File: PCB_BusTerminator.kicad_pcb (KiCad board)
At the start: 2 copper layers, 16 x 33 mm, 5 parts, among them J1 Interconnect Bus

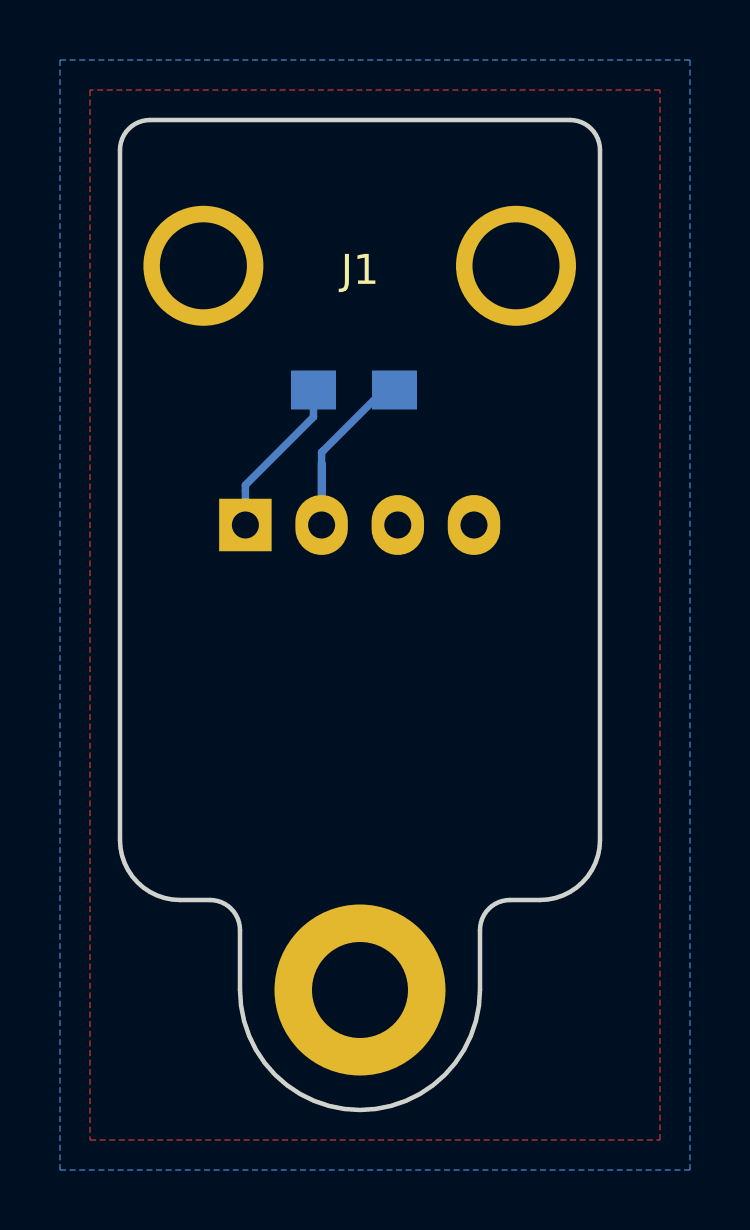
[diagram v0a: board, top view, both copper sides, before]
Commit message: Move top edge closer to connector
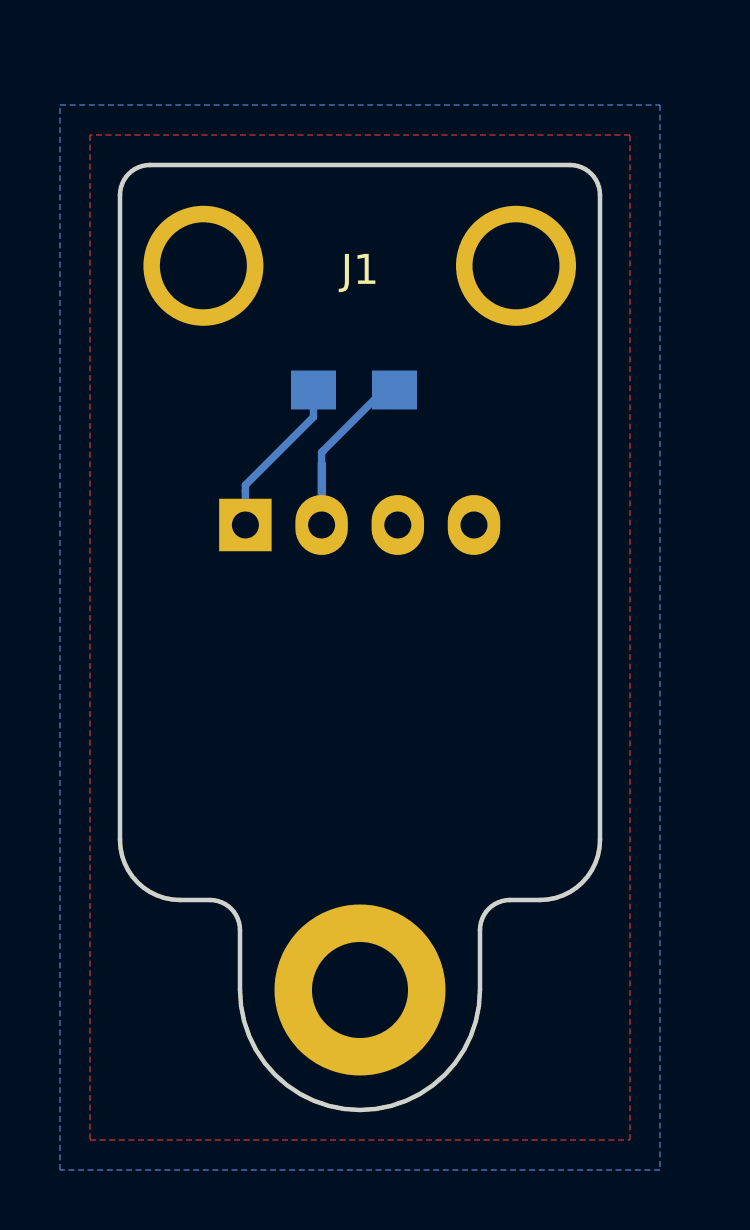
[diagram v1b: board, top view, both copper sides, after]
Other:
- board size 16 x 33 mm -> 16 x 31.5 mm
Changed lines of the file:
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@@
     (links 2)
     (no_connects 0)
-    (area 143.924999 107.924999 160.075001 141.075001)
+    (area 143.924999 109.424999 160.075001 141.075001)
     (thickness 1.6)
     (drawings 15)
@@
     (effects (font (size 1.1 1.1) (thickness 0.2)) (justify mirror))
   )
-  (gr_arc (start 145 109) (end 144 109) (angle 90) (layer Edge.Cuts) (width 0.15))
-  (gr_arc (start 159 109) (end 159 108) (angle 90) (layer Edge.Cuts) (width 0.15))
+  (gr_arc (start 145 110.5) (end 144 110.5) (angle 90) (layer Edge.Cuts) (width 0.15))
+  (gr_arc (start 159 110.5) (end 159 109.5) (angle 90) (layer Edge.Cuts) (width 0.15))
   (gr_arc (start 146 132) (end 146 134) (angle 90) (layer Edge.Cuts) (width 0.15))
-  (gr_line (start 144 132) (end 144 109) (layer Edge.Cuts) (width 0.15))
-  (gr_line (start 160 109) (end 160 132) (layer Edge.Cuts) (width 0.15))
-  (gr_line (start 145 108) (end 159 108) (layer Edge.Cuts) (width 0.15))
+  (gr_line (start 144 132) (end 144 110.5) (layer Edge.Cuts) (width 0.15))
+  (gr_line (start 160 110.5) (end 160 132) (layer Edge.Cuts) (width 0.15))
+  (gr_line (start 145 109.5) (end 159 109.5) (layer Edge.Cuts) (width 0.15))
   (segment (start 150.768205 119.031795) (end 150.72 119.08) (width 0.25) (layer B.Cu) (net 2))
   (segment (start 150.72 119.08) (end 150.72 121.5) (width 0.25) (layer B.Cu) (net 2))
@@
     (polygon
       (pts
-        (xy 143 107) (xy 143 142) (xy 162 142) (xy 162 107)
+        (xy 143 108.5) (xy 143 142) (xy 161 142) (xy 161 108.5)
       )
     )
@@
     (polygon
       (pts
-        (xy 142 106) (xy 163 106) (xy 163 143) (xy 142 143)
+        (xy 142 107.5) (xy 162 107.5) (xy 162 143) (xy 142 143)
       )
     )
